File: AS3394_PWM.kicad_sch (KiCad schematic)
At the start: 88 parts

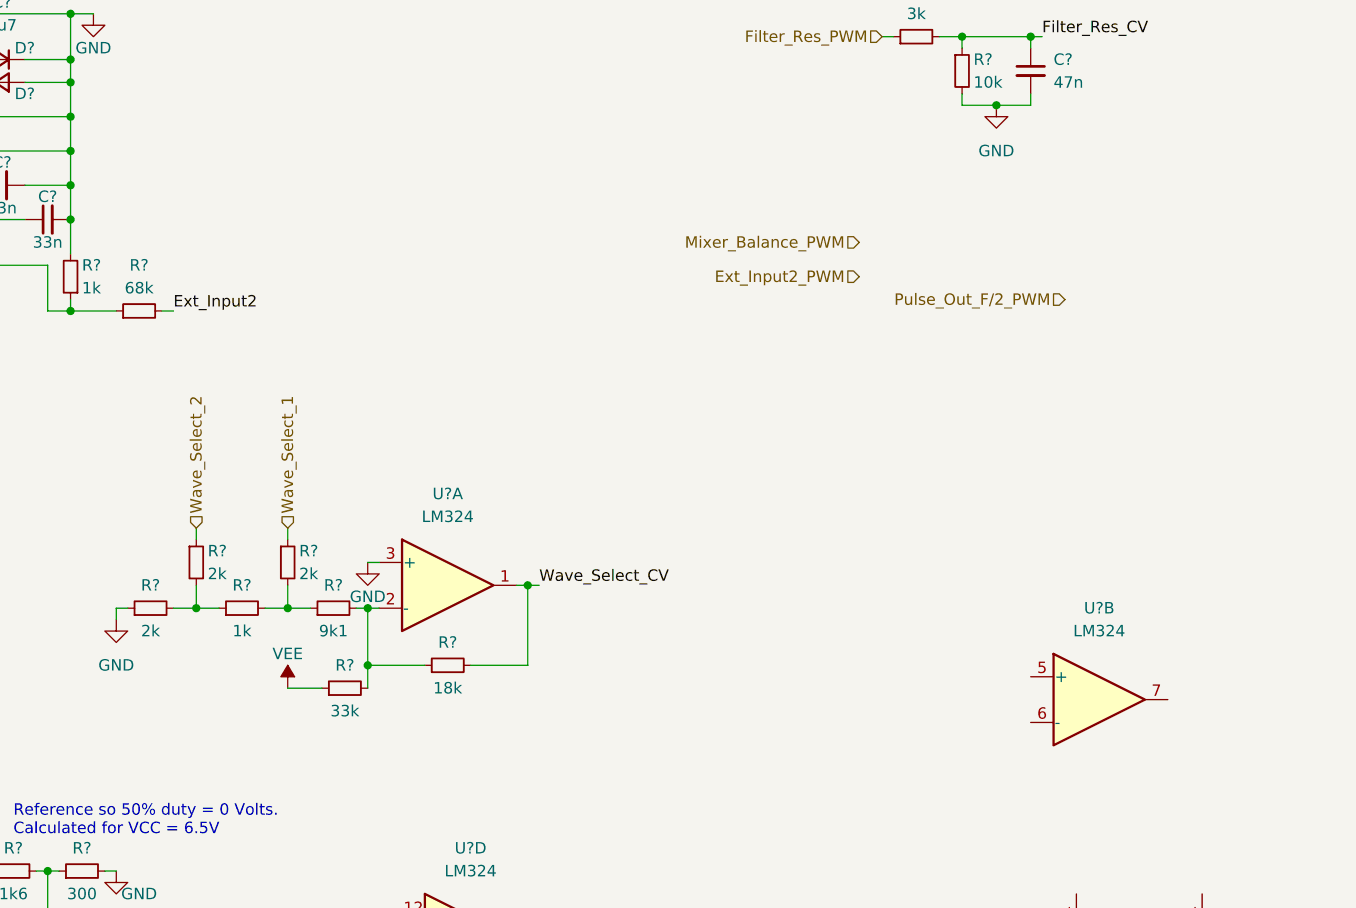
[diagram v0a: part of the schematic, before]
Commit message: Finished schema; decided to make voice cards mono and leave stereo mixing to mainboards instead
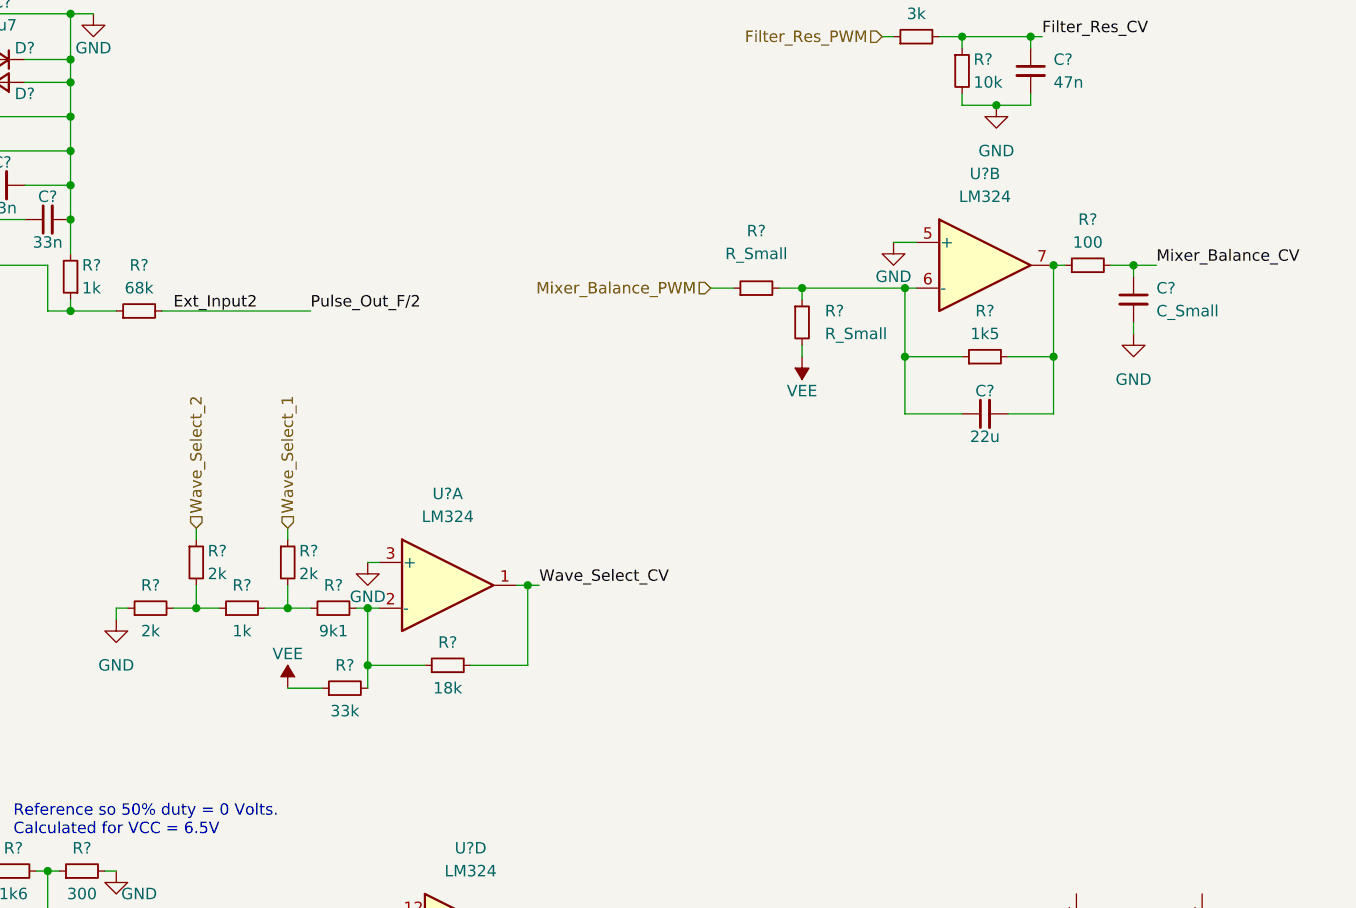
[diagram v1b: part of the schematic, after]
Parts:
- added C?: C_Small, symbol Device:C_Small
- added C?: 22u, symbol Device:C_Small
- added R? (x2): R_Small, symbol Device:R_Small
- added R?: 1k5, symbol Device:R_Small
- added R?: 100, symbol Device:R_Small
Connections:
- net Pulse_Out_F/2 is gone; now on net Ext_Input2: U?.5 (Pulse_Out_F/2)
- net GND: now also U?.5 (+), C?.2
- net Mixer_Balance_CV: now also C?.1, R?.2
- net Mixer_Balance_PWM: now also R?.1
- net VEE: now also R?.2
- net at U?.6 (-): now also C?.1, R?.1, R?.1, R?.2
- net at U?.7: now also C?.2, R?.1, R?.2
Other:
- moved on the sheet: U?B

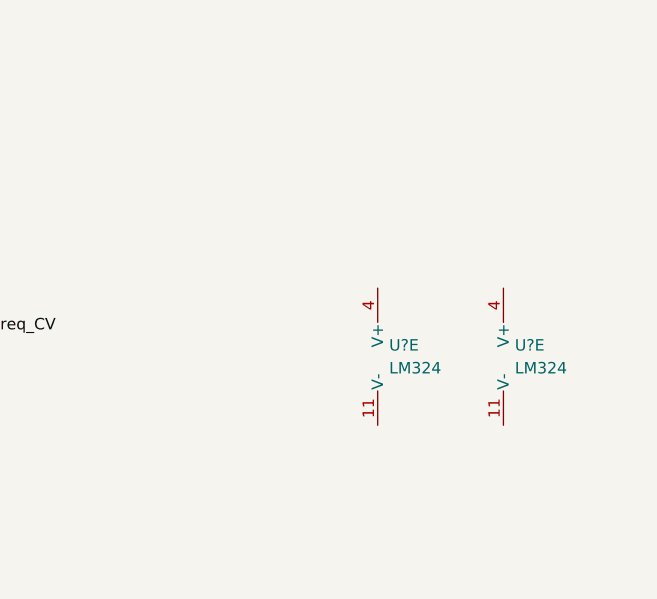
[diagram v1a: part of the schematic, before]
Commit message: Last commit was a lie. Added bypass caps and power conns to LM324s.
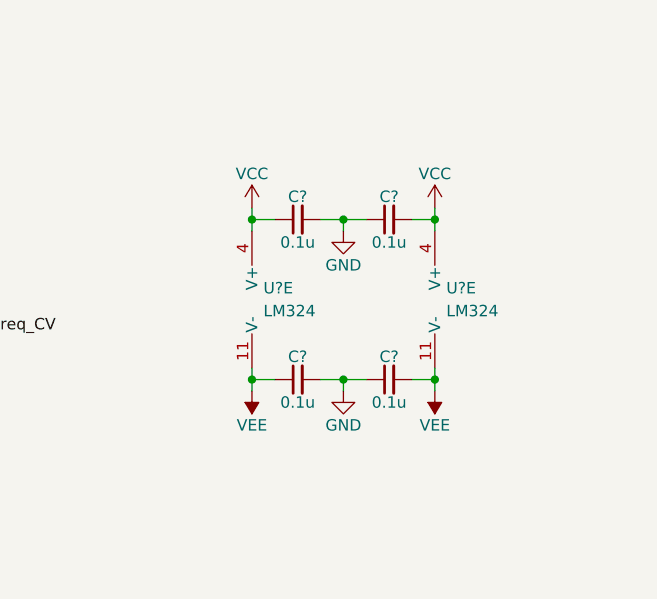
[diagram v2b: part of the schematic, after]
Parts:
- added C? (x4): 0.1u, symbol Device:C_Small
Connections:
- net GND: now also C?.1, C?.1, C?.2, C?.2
- net VCC: now also U?.4 (V+), U?.4 (V+), C?.1, C?.2
- net VEE: now also U?.11 (V-), U?.11 (V-), C?.1, C?.2
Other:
- moved on the sheet: U?E

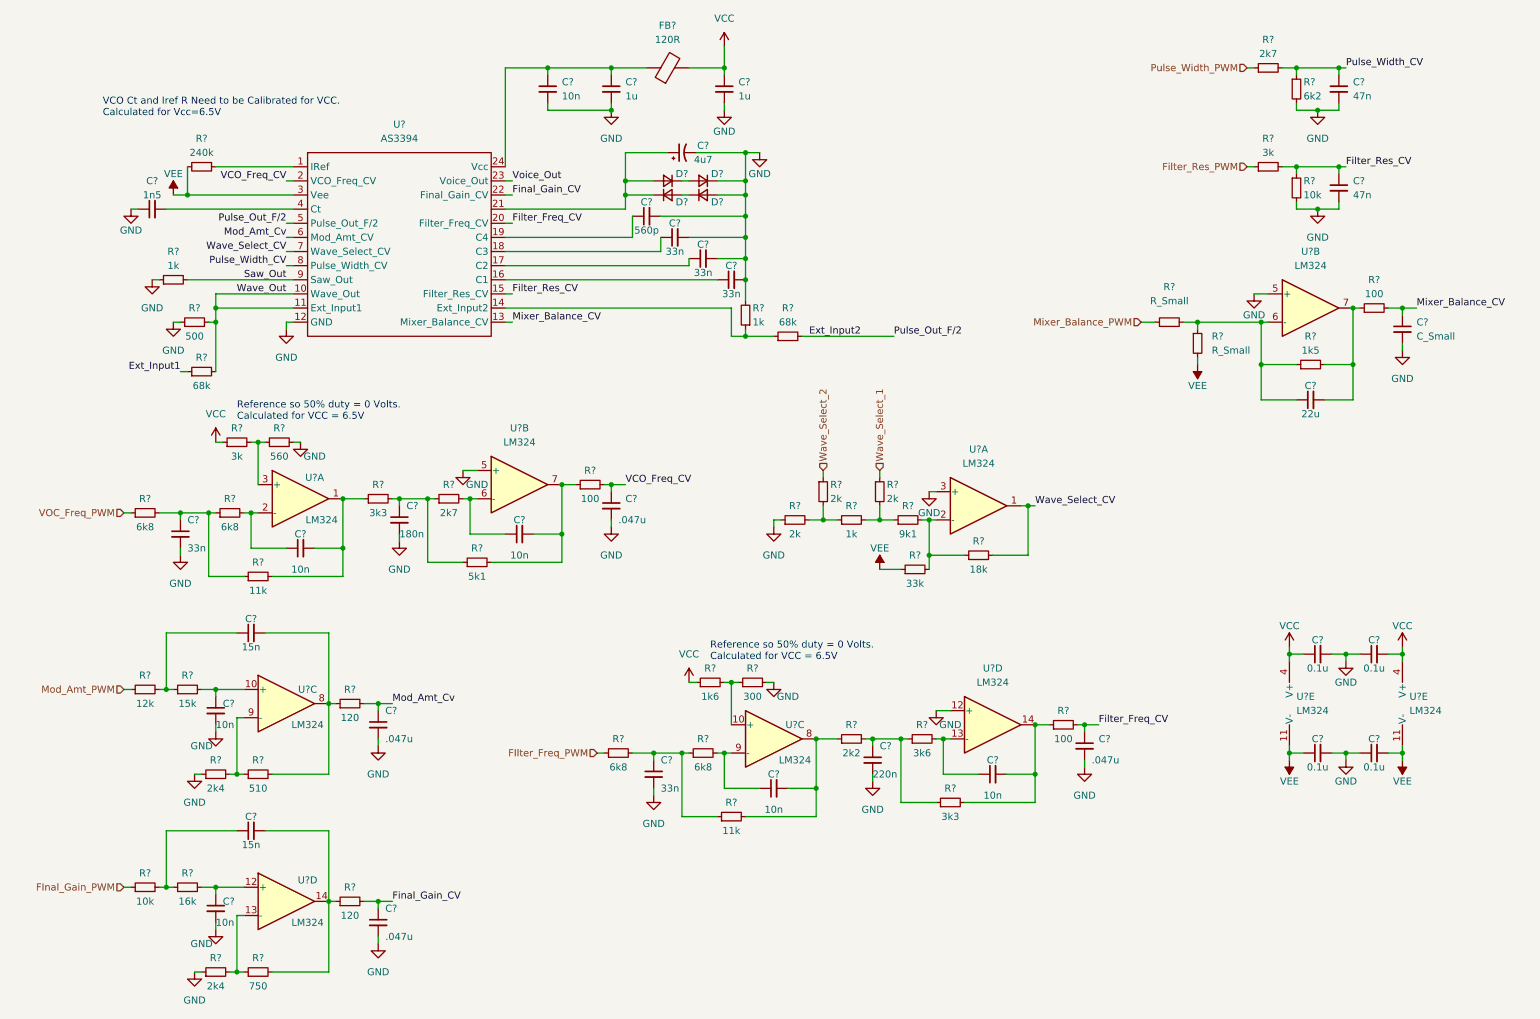
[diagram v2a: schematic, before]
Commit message: Added PWM connections from RP2040 to subsheet containing AS3394; finished assinging components for JLC assembly
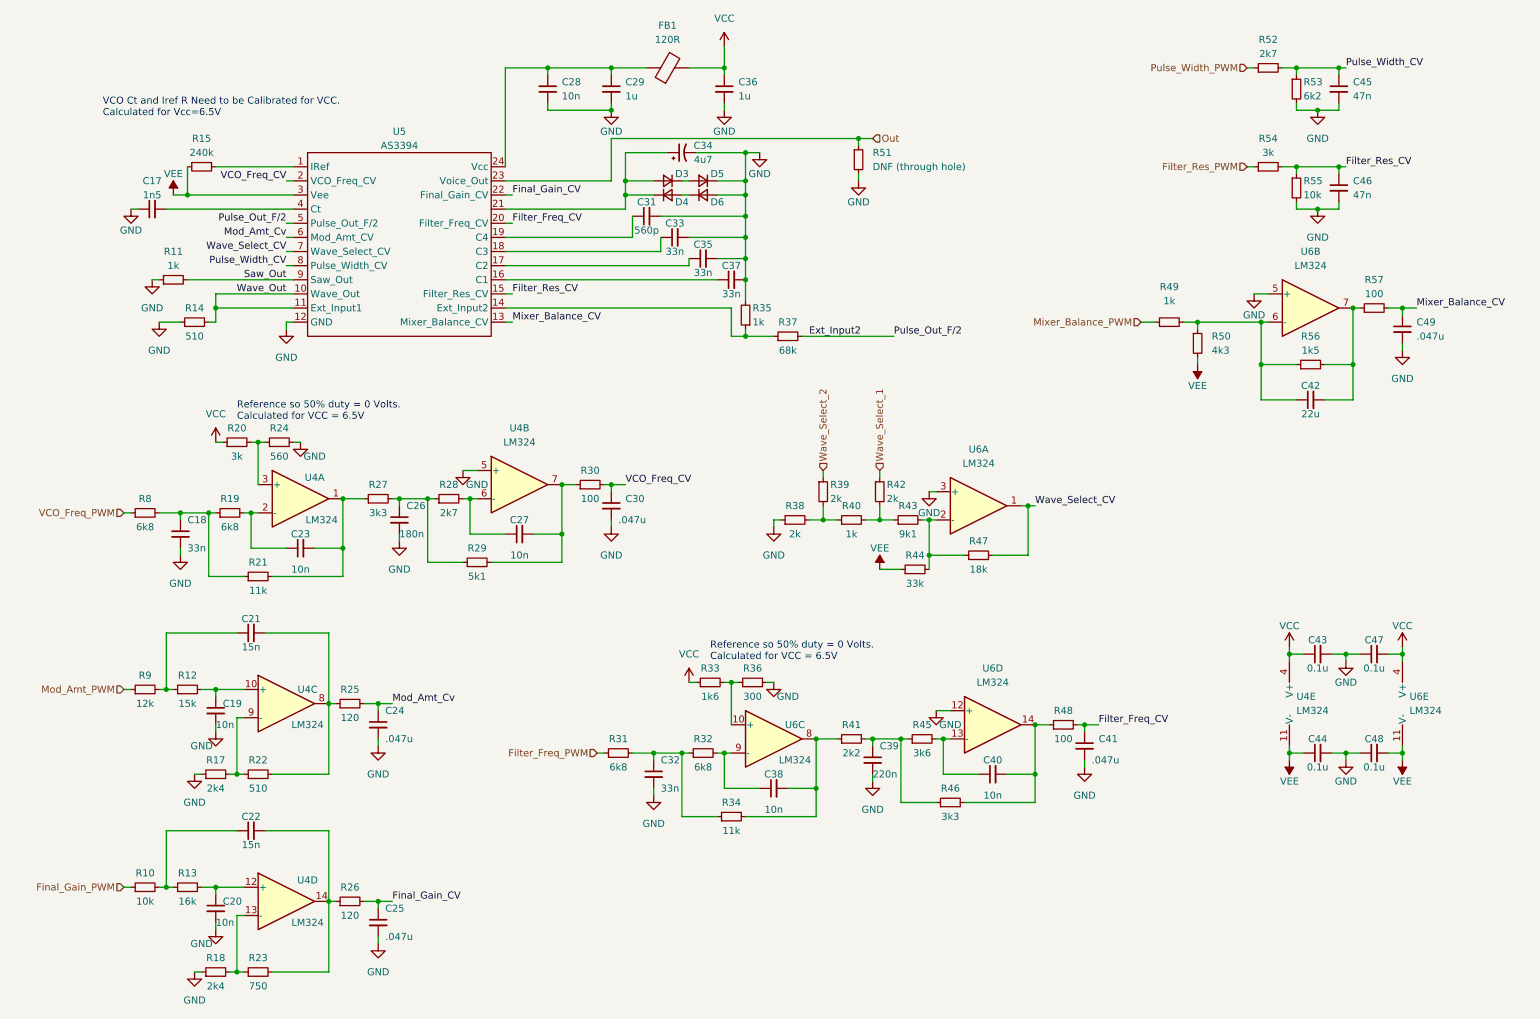
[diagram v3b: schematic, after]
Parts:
- removed R?: 68k, symbol Device:R_Small
- added R51: DNF (through hole), Resistor_SMD:R_0603_1608Metric, symbol Device:R_Small
- C17, C18, C21, C22, C24, C25, C30, C32, C33, C35, C37, C41, C45, C46: renamed from C?; footprint (none) -> Capacitor_SMD:C_0603_1608Metric
- C19, C23, C27, C28, C29, C31, C36, C38, C39, C40, C43, C44, C47, C48: renamed from C?; footprint (none) -> Capacitor_SMD:C_0402_1005Metric
- C20: renamed from C?; footprint (none) -> Capacitor_SMD:C_01005_0402Metric
- C26: renamed from C?; footprint (none) -> Capacitor_SMD:C_0805_2012Metric
- C34: renamed from C?; footprint (none) -> Capacitor_SMD:CP_Elec_4x5.4
- C42: renamed from C?; footprint (none) -> Capacitor_SMD:C_1206_3216Metric
- C49: renamed from C?; value C_Small -> .047u; footprint (none) -> Capacitor_SMD:C_0603_1608Metric
- D3, D4, D5, D6: renamed from D?; footprint (none) -> Diode_SMD:D_SMA
- FB1: renamed from FB?; footprint (none) -> Inductor_SMD:L_0805_2012Metric
- R10, R11, R12, R17, R18, R19, R22, R25, R26, R27, R29, R30, R31, R32, R33, R35, R36, R37, R38, R39, R40, R41, R42, R46, R47, R48, R55, R56, R57, R8, R9: renamed from R?; footprint (none) -> Resistor_SMD:R_0402_1005Metric
- R13: renamed from R?; footprint (none) -> Resistor_SMD:R_0805_2012Metric
- R14: renamed from R?; value 500 -> 510; footprint (none) -> Resistor_SMD:R_0402_1005Metric
- R15, R21, R23, R24, R28, R34, R43, R45, R52, R53, R54: renamed from R?; footprint (none) -> Resistor_SMD:R_0603_1608Metric
- R20: renamed from R?; footprint (none) -> Resistor_SMD:R_0201_0603Metric
- R44: renamed from R?; footprint (none) -> Resistor_SMD:R_01005_0402Metric
- R49: renamed from R?; value R_Small -> 1k; footprint (none) -> Resistor_SMD:R_0402_1005Metric
- R50: renamed from R?; value R_Small -> 4k3; footprint (none) -> Resistor_SMD:R_0603_1608Metric
- U4, U6: renamed from U?; footprint (none) -> Package_SO:SOIC-14_3.9x8.7mm_P1.27mm
- U5: renamed from U?; footprint (none) -> Package_DIP:DIP-24_W7.62mm_Socket
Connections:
- net GND: now also R51.2
- net FIlter_Freq_PWM renamed Filter_Freq_PWM
- net FInal_Gain_PWM renamed Final_Gain_PWM
- net VOC_Freq_PWM renamed VCO_Freq_PWM
- net Voice_Out renamed Out
- net Out: now also R51.1

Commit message: Started placement
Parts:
- renumbered U6 to U4, U4 to U6
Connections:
- net GND: now also U4.12 (+); no longer U4.3 (+)
- net Wave_Select_CV: now also U4.14; no longer U4.1
- net at R18.2, R23.1: now also U6.2 (-); no longer U6.13 (-)
- net at C22.2, R23.2, R26.1: now also U6.1; no longer U6.14
- net at R43.2, R44.2, R47.1: now also U4.13 (-); no longer U4.2 (-)
- net at C20.1, R13.2: now also U6.3 (+); no longer U6.12 (+)
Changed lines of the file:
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@@
     (pin "2")
   )
-  (symbol (lib_id "Amplifier_Operational:LM324") (at 60.96 177.8 0) (unit 4)
-    (in_bom yes) (on_board yes)
-    (property "Reference" "U4" (id 0) (at 64.77 173.99 0))
+  (symbol (lib_id "Amplifier_Operational:LM324") (at 60.96 177.8 0) (unit 1)
+    (in_bom yes) (on_board yes)
+    (property "Reference" "U6" (id 0) (at 64.77 173.99 0))
     (property "Value" "LM324" (id 1) (at 64.77 181.61 0))
     (property "Footprint" "Package_SO:SOIC-14_3.9x8.7mm_P1.27mm" (id 2) (at 59.69 175.26 0)
@@
     (pin "2")
   )
-  (symbol (lib_id "Amplifier_Operational:LM324") (at 185.42 106.68 0) (unit 1)
-    (in_bom yes) (on_board yes) (fields_autoplaced)
-    (property "Reference" "U6" (id 0) (at 185.42 96.52 0))
+  (symbol (lib_id "Amplifier_Operational:LM324") (at 185.42 106.68 0) (unit 4)
+    (in_bom yes) (on_board yes) (fields_autoplaced)
+    (property "Reference" "U4" (id 0) (at 185.42 96.52 0))
     (property "Value" "LM324" (id 1) (at 185.42 99.06 0))
     (property "Footprint" "Package_SO:SOIC-14_3.9x8.7mm_P1.27mm" (id 2) (at 184.15 104.14 0)
